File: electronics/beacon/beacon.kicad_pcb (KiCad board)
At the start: 2 copper layers, 20.8 x 9.6 mm, 15 parts, among them J1 CONN_01X04, J2 CONN_01X04, J3 Rails, Q1 Q_NMOS_GSD, U1 ATTINY45-20XUR, U2 TPS70928DBV

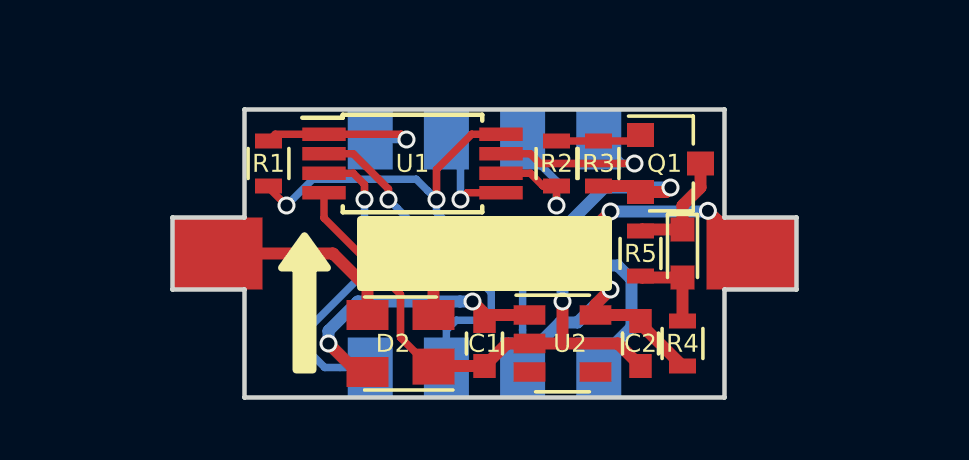
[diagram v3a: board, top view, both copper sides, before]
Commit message: electronics: beacon: Final beacon board Rev 1.1
- widened track solder tabs
- improved schematic/board images
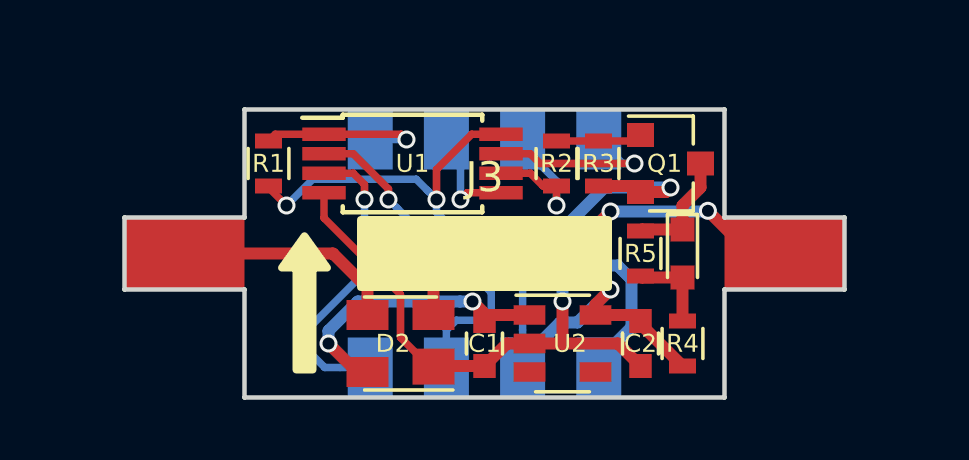
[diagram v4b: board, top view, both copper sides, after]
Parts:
- J3: footprint bcan:HO_Rail_2_Length2.4mm_Width3mm -> bcan:HO_Rail_2_Length2.4mm_Width4mm
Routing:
- net Net-(D2-Pad3): track 6.38 -> 7.48 mm
- net Net-(D2-Pad2): track 14.0 -> 15.1 mm
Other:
- board size 20.8 x 9.6 mm -> 24 x 9.6 mm
- board text added: "Rev 1.1"
- board text added: "bcan.io"
- board text removed: "Rev 1.0"
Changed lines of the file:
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@@
     (links 30)
     (no_connects 0)
-    (area 139.524999 100.124999 160.475001 109.875001)
+    (area 137.8 96.166666 162.2 113.833333)
     (thickness 0.8)
-    (drawings 25)
-    (tracks 147)
+    (drawings 26)
+    (tracks 146)
     (zones 0)
     (modules 15)
@@
   )
   (page A4)
+  (title_block
+    (title "IR Beacon Board")
+    (date 2017-03-16)
+    (rev 1.1)
+    (company "ECE 445")
+  )
   (layers
     (0 F.Cu signal)
@@
       (plotinvisibletext false)
       (padsonsilk false)
-      (subtractmaskfromsilk true)
+      (subtractmaskfromsilk false)
       (outputformat 1)
       (mirror false)
       (drillshape 0)
       (scaleselection 1)
-      (outputdirectory gerbers))
+      (outputdirectory images))
   )
   (net 0 "")
@@
     )
   )
-  (module bcan:HO_Rail_2_Length2.4mm_Width3mm (layer F.Cu)
-    (at 150 105)
-    (fp_text reference J3 (at 0 -2.54) (layer F.SilkS) hide
-      (effects (font (size 1 1) (thickness 0.15)))
-    )
-    (fp_text value Rails (at 0 2.54) (layer F.Fab)
-      (effects (font (size 1 1) (thickness 0.15)))
-    )
-    (pad 1 smd rect (at -8.9 0) (size 3 2.4) (layers F.Cu F.Mask)
-      (net 16 "Net-(D2-Pad3)"))
-    (pad 2 smd rect (at 8.9 0) (size 3 2.4) (layers F.Cu F.Mask)
-      (net 15 "Net-(D2-Pad2)"))
-    (pad "" np_thru_hole circle (at 0 0) (size 1 1) (drill 1) (layers *.Cu *.Mask))
-  )
   (module Resistors_SMD:R_0603 (layer F.Cu)
     (at 155.2 105 90)
@@
       (net 1 GND))
   )
+  (module bcan:HO_Rail_2_Length2.4mm_Width4mm (layer F.Cu)
+    (at 150 105)
+    (fp_text reference J3 (at 0 -2.54) (layer F.SilkS)
+      (effects (font (size 1 1) (thickness 0.15)))
+    )
+    (fp_text value Rails (at 0 2.54) (layer F.Fab)
+      (effects (font (size 1 1) (thickness 0.15)))
+    )
+    (pad 1 smd rect (at -10 0) (size 4 2.4) (layers F.Cu F.Mask)
+      (net 16 "Net-(D2-Pad3)"))
+    (pad 2 smd rect (at 10 0) (size 4 2.4) (layers F.Cu F.Mask)
+      (net 15 "Net-(D2-Pad2)"))
+    (pad "" np_thru_hole circle (at 0 0) (size 1 1) (drill 1) (layers *.Cu *.Mask))
+  )
+  (gr_text bcan.io (at 143.2 105 90) (layer B.SilkS)
+    (effects (font (size 1.5 1.5) (thickness 0.3)) (justify mirror))
+  )
   (gr_line (start 144.4 109.8) (end 144.4 100.2) (layer B.SilkS) (width 0.2))
   (gr_line (start 155.6 105) (end 144.4 105) (layer B.SilkS) (width 0.2))
   (gr_line (start 155.6 100.2) (end 155.6 109.8) (layer B.SilkS) (width 0.2))
-  (gr_text R (at 158.9 105) (layer B.SilkS)
-    (effects (font (size 1.5 1.5) (thickness 0.3)) (justify mirror))
-  )
-  (gr_text L (at 141.1 105) (layer B.SilkS)
-    (effects (font (size 1.5 1.5) (thickness 0.3)) (justify mirror))
-  )
-  (gr_text "Rev 1.0" (at 157 100.8 90) (layer B.SilkS)
+  (gr_text R (at 160 105) (layer B.SilkS)
+    (effects (font (size 1.5 1.5) (thickness 0.3)) (justify mirror))
+  )
+  (gr_text L (at 140 105) (layer B.SilkS)
+    (effects (font (size 1.5 1.5) (thickness 0.3)) (justify mirror))
+  )
+  (gr_text "Rev 1.1" (at 157 100.8 90) (layer B.SilkS)
     (effects (font (size 1.5 1.5) (thickness 0.3)) (justify left mirror))
   )
@@
   )
   (gr_line (start 142 103.8) (end 142 100.2) (layer Edge.Cuts) (width 0.15))
-  (gr_line (start 139.6 103.8) (end 142 103.8) (layer Edge.Cuts) (width 0.15))
-  (gr_line (start 139.6 106.2) (end 139.6 103.8) (layer Edge.Cuts) (width 0.15))
-  (gr_line (start 142 106.2) (end 139.6 106.2) (layer Edge.Cuts) (width 0.15))
+  (gr_line (start 138 103.8) (end 142 103.8) (layer Edge.Cuts) (width 0.15))
+  (gr_line (start 138 106.2) (end 138 103.8) (layer Edge.Cuts) (width 0.15))
+  (gr_line (start 142 106.2) (end 138 106.2) (layer Edge.Cuts) (width 0.15))
   (gr_line (start 142 109.8) (end 142 106.2) (layer Edge.Cuts) (width 0.15))
   (gr_line (start 158 106.2) (end 158 109.8) (layer Edge.Cuts) (width 0.15))
-  (gr_line (start 160.4 106.2) (end 158 106.2) (layer Edge.Cuts) (width 0.15))
-  (gr_line (start 160.4 103.8) (end 160.4 106.2) (layer Edge.Cuts) (width 0.15))
-  (gr_line (start 158 103.8) (end 160.4 103.8) (layer Edge.Cuts) (width 0.15))
+  (gr_line (start 162 106.2) (end 158 106.2) (layer Edge.Cuts) (width 0.15))
+  (gr_line (start 162 103.8) (end 162 106.2) (layer Edge.Cuts) (width 0.15))
+  (gr_line (start 158 103.8) (end 162 103.8) (layer Edge.Cuts) (width 0.15))
   (gr_line (start 158 100.2) (end 158 103.8) (layer Edge.Cuts) (width 0.15))
   (gr_line (start 158 109.8) (end 142 109.8) (layer Edge.Cuts) (width 0.15))
@@
   (segment (start 145.75 108.95) (end 144.8 108) (width 0.4) (layer F.Cu) (net 14))
   (segment (start 151.5 107.05) (end 150.2 107.05) (width 0.4) (layer F.Cu) (net 14))
+  (segment (start 160 105) (end 158.870836 105) (width 0.4) (layer F.Cu) (net 15))
+  (segment (start 158.870836 105) (end 157.447223 103.576387) (width 0.4) (layer F.Cu) (net 15))
   (segment (start 154.2 103.6) (end 153.4 104.4) (width 0.4) (layer F.Cu) (net 15))
   (segment (start 153.4 104.4) (end 150.732002 104.4) (width 0.4) (layer F.Cu) (net 15))
@@
   (segment (start 148.3 107.05) (end 148.3 105.367998) (width 0.4) (layer F.Cu) (net 15))
   (segment (start 148.3 105.367998) (end 149.667998 104) (width 0.4) (layer F.Cu) (net 15))
-  (segment (start 158.870836 105) (end 157.747222 103.876386) (width 0.4) (layer F.Cu) (net 15))
-  (segment (start 157.747222 103.876386) (end 157.447223 103.576387) (width 0.4) (layer F.Cu) (net 15))
-  (segment (start 158.9 105) (end 158.870836 105) (width 0.4) (layer F.Cu) (net 15))
   (segment (start 157.4 103.529164) (end 157.447223 103.576387) (width 0.4) (layer F.Cu) (net 15))
   (segment (start 157.4 103.5) (end 157.4 103.529164) (width 0.4) (layer F.Cu) (net 15))
@@
   (via (at 157.447223 103.576387) (size 0.6) (drill 0.4) (layers F.Cu B.Cu) (net 15))
   (via (at 154.2 103.6) (size 0.6) (drill 0.4) (layers F.Cu B.Cu) (net 15))
+  (segment (start 140 105) (end 144.95 105) (width 0.4) (layer F.Cu) (net 16))
   (segment (start 144.95 105) (end 146.1 106.15) (width 0.4) (layer F.Cu) (net 16))
-  (segment (start 141.1 105) (end 144.95 105) (width 0.4) (layer F.Cu) (net 16))
   (segment (start 146.1 106.15) (end 146.1 107.05) (width 0.4) (layer F.Cu) (net 16))
   (zone (net 1) (net_name GND) (layer F.Cu) (hatch edge 0.508)
@@
     (polygon
       (pts
-        (xy 158 109.8) (xy 142 109.8) (xy 142 106.2) (xy 139.6 106.2) (xy 139.6 103.8)
-        (xy 142 103.8) (xy 142 100.2) (xy 158 100.2) (xy 158 103.8) (xy 160.4 103.8)
-        (xy 160.4 106.2) (xy 158 106.2)
+        (xy 158 109.8) (xy 142 109.8) (xy 142 106.2) (xy 138 106.2) (xy 138 103.8)
+        (xy 142 103.8) (xy 142 100.2) (xy 158 100.2) (xy 158 103.8) (xy 162 103.8)
+        (xy 162 106.2) (xy 158 106.2)
       )
     )
@@
     (polygon
       (pts
-        (xy 158 109.8) (xy 142 109.8) (xy 142 106.2) (xy 139.6 106.2) (xy 139.6 103.8)
-        (xy 142 103.8) (xy 142 100.2) (xy 158 100.2) (xy 158 103.8) (xy 160.4 103.8)
-        (xy 160.4 106.2) (xy 158 106.2)
+        (xy 158 109.8) (xy 142 109.8) (xy 142 106.2) (xy 138 106.2) (xy 138 103.8)
+        (xy 142 103.8) (xy 142 100.2) (xy 158 100.2) (xy 158 103.8) (xy 162 103.8)
+        (xy 162 106.2) (xy 158 106.2)
       )
     )
